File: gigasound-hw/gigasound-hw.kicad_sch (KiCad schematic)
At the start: 14 parts, among them J1 Conn_01x04_Socket, J2 Conn_01x05_Socket, SW1 PLAY, SW2 STOP, SW3 MODE, U1 STM32F401RETx, Y1 8MHz

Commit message: progress hw schematic
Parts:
- removed SW3: MODE, symbol Switch:SW_Push
- added C10: C, symbol Device:C
- added C11, C3, C4, C5, C6, C7, C8, C9: 100nF, symbol Device:C
- added C12: 4.7uF, symbol Device:C
- added J3: Conn_01x05_Socket, symbol Connector:Conn_01x05_Socket
- added L1: 600R, symbol Device:L
- added R3, R4, R5, R6: 10K, symbol Device:R
- added SW4: STOP, symbol Switch:SW_Push
- added SW5: MODE, symbol Switch:SW_Push
- added TPA8, TPB1, TPB10, TPB12, TPB2, TPB3, TPB4, TPB5, TPB8, TPB9, TPC0, TPC1, TPC10, TPC11, TPC12, TPC13, TPC14, TPC15, TPC2, TPC3, TPC6, TPC7, TPC8, TPC9, TPD2: ~, TestPoint:TestPoint_Pad_D1.0mm, symbol Connector:TestPoint
- SW2: value STOP -> 100nF
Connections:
- net GND: now also D1.3 (VSS), SW1.1, SW2.1, U1.12 (VSSA), U1.18 (VSS), U1.31 (VSS), U1.47 (VSS), U1.63 (VSS), C10.1, C11.1, C12.1, C3.2, C4.2, C5.2, J3.GND, R6.1, SW4.1, SW5.1
- net 5V: now reaches D1.1 (VDD)
- net LED: now reaches D1.4 (DIN)
- net LED: now also U1.50 (PA15)
- net PLAY: now reaches SW1.2
- net PLAY: now also U1.34 (PB13), C3.1
- net at SW2.2: now also U1.7 (NRST), C10.2
- net at R1.1: now also R3.2
- net at U1.1 (VBAT): now also U1.19 (VDD), U1.32 (VDD), U1.48 (VDD), U1.64 (VDD), C6.2, C7.2, C8.2, C9.2
- net at U1.10 (PC2): now also TPC2.1
- net at U1.11 (PC3): now also TPC3.1
- net VDDA: now reaches U1.13 (VREF+)
- net VDDA: now also C11.2, L1.1
- net ADC_CH0: now reaches U1.14 (PA0)
- net ADC_CH1: now reaches U1.15 (PA1)
- net ADC_CH2: now reaches U1.16 (PA2)
- net ADC_CH3: now reaches U1.17 (PA3)
- net at U1.2 (PC13): now also TPC13.1
- net ADC_CH4: now reaches U1.20 (PA4)
- net ADC_CH5: now reaches U1.21 (PA5)
- net ADC_CH6: now reaches U1.22 (PA6)
- net ADC_CH7: now reaches U1.23 (PA7)
- net ADC_CH14: now reaches U1.24 (PC4)
- net ADC_CH15: now reaches U1.25 (PC5)
- net ADC_CH8: now reaches U1.26 (PB0)
- net at U1.27 (PB1): now also TPB1.1
- net at U1.28 (PB2): now also TPB2.1
- net at U1.29 (PB10): now also TPB10.1
- net at U1.3 (PC14): now also TPC14.1
- net at U1.30 (VCAP1): now also C12.2
- net at U1.33 (PB12): now also TPB12.1
- net STOP: now reaches U1.35 (PB14)
- net STOP: now also C4.1, SW4.2
- net MODE: now reaches U1.36 (PB15)
- net MODE: now also C5.1, SW5.2
- net at U1.37 (PC6): now also TPC6.1
- net at U1.38 (PC7): now also TPC7.1
- net at U1.39 (PC8): now also TPC8.1
- net at U1.4 (PC15): now also TPC15.1
- net at U1.40 (PC9): now also TPC9.1
- net at U1.41 (PA8): now also TPA8.1
- net TX: now reaches U1.42 (PA9)
- net TX: now also J3.TX
- net RX: now reaches U1.43 (PA10)
- net RX: now also J3.RX
- net USB_DM: now reaches U1.44 (PA11)
- net USB_DP: now reaches U1.45 (PA12)
- net SWDIO: now reaches U1.46 (PA13)
- net SWDIO: now also J3.SWDIO
- net SWCLK: now reaches U1.49 (PA14)
- net SWCLK: now also J3.SWCLK
- net at U1.51 (PC10): now also TPC10.1
- net at U1.52 (PC11): now also TPC11.1
- net at U1.53 (PC12): now also TPC12.1
- net at U1.54 (PD2): now also TPD2.1
- net at U1.55 (PB3): now also TPB3.1
- net at U1.56 (PB4): now also TPB4.1
- net at U1.57 (PB5): now also TPB5.1
- net SCL: now reaches U1.58 (PB6)
- net SCL: now also R5.2
- net SDA: now reaches U1.59 (PB7)
- net SDA: now also R4.2
- net at U1.60 (BOOT0): now also R6.2
- net at U1.61 (PB8): now also TPB8.1
- net at U1.62 (PB9): now also TPB9.1
- net at U1.8 (PC0): now also TPC0.1
- net at U1.9 (PC1): now also TPC1.1
- new net 3.3V: C6.1, C7.1, C8.1, C9.1, L1.2, R3.1, R4.1, R5.1
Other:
- note added: "UART DEBUG PORT PROGRAMMING PORT"
- company: (none) -> Poliba
- title: (none) -> GigaSound-MIDI
- moved on the sheet: C1, C2, D1, J2, R1, R2, SW1, Y1

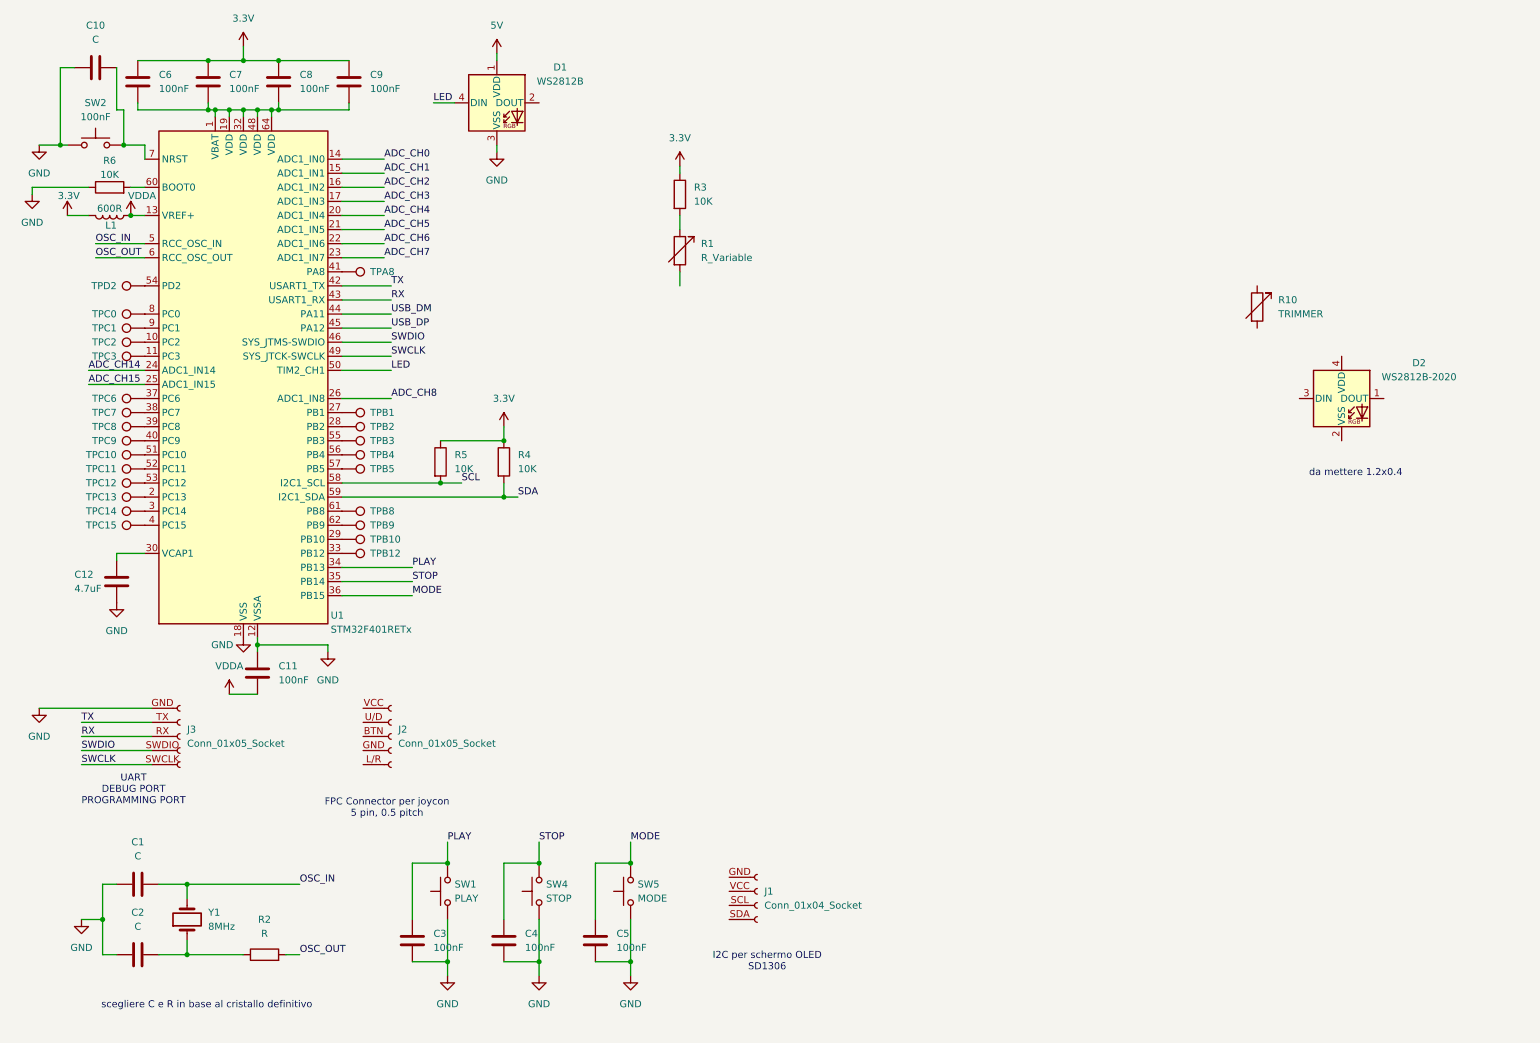
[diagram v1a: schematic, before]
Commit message: hw: added usb, 3.3v, cleaned up
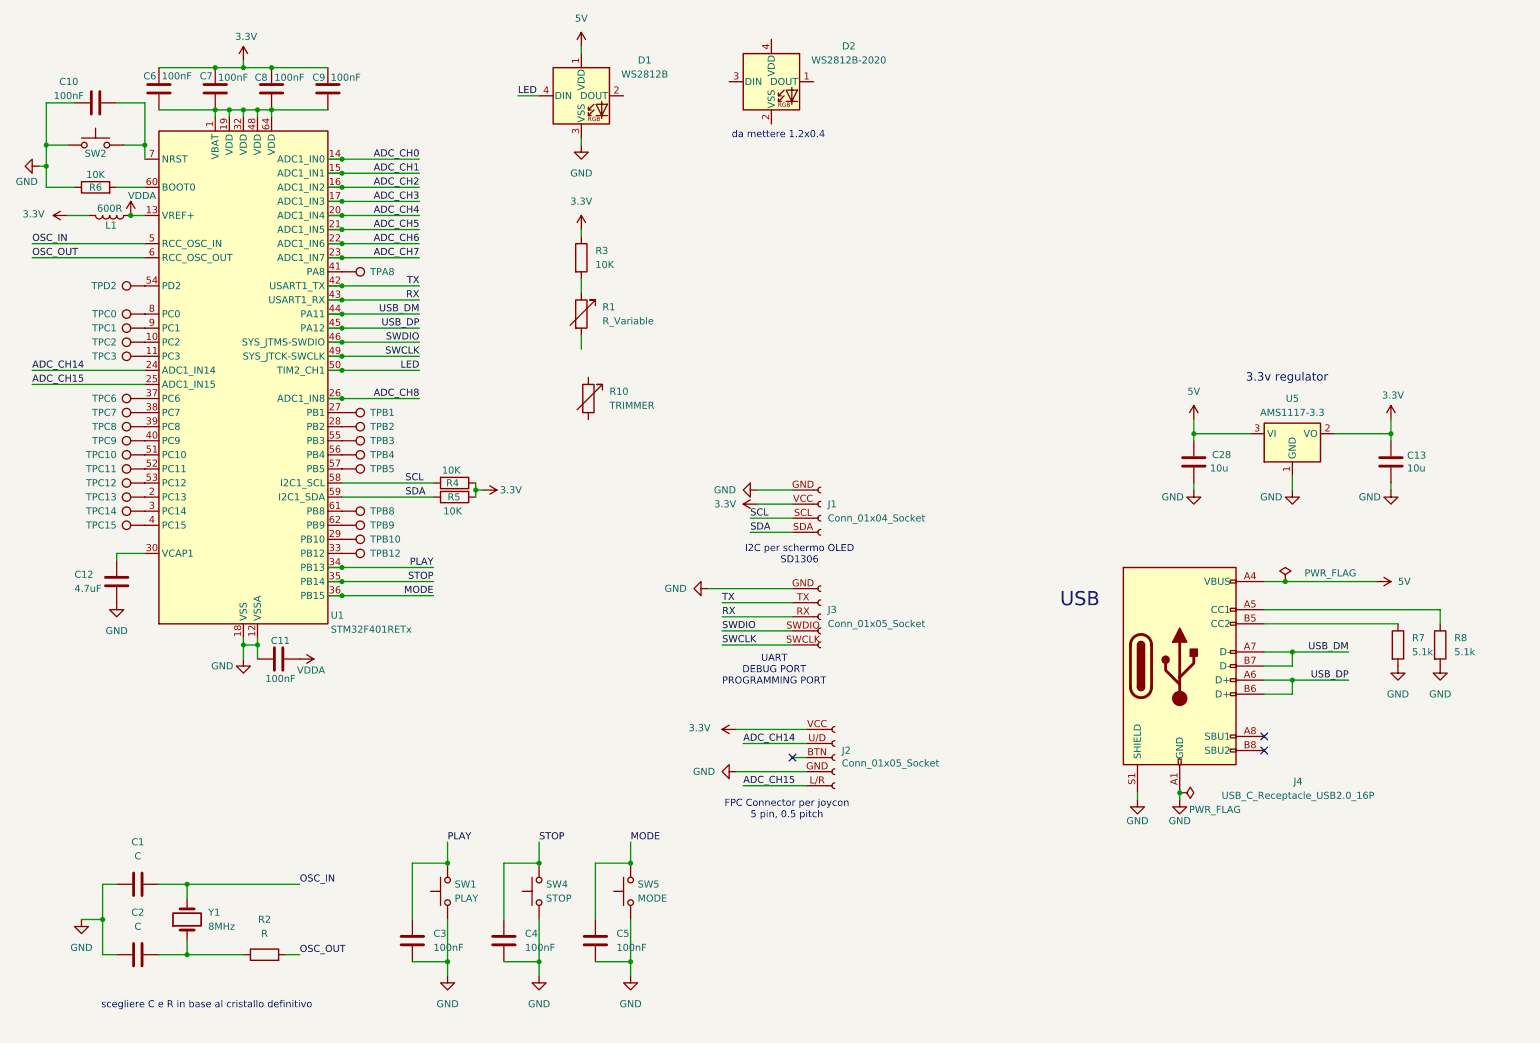
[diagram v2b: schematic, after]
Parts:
- added C13, C28: 10u, Capacitor_SMD:C_0402_1005Metric_Pad0.74x0.62mm_HandSolder, symbol Device:C
- added J4: USB_C_Receptacle_USB2.0_16P, Connector_USB:USB_C_Receptacle_G-Switch_GT-USB-7010ASV, symbol Connector:USB_C_Receptacle_USB2.0_16P
- added R7, R8: 5.1k, Resistor_SMD:R_0402_1005Metric_Pad0.72x0.64mm_HandSolder, symbol Device:R
- added U5: AMS1117-3.3, Package_TO_SOT_SMD:SOT-223-3_TabPin2, symbol Regulator_Linear:AMS1117-3.3
- C10: value C -> 100nF
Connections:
- net 3.3V: now also J1.VCC, J2.VCC, C13.1, U5.2 (VO)
- net 5V: now also C28.1, J4.A4 (VBUS), J4.A9 (VBUS), J4.B4 (VBUS), J4.B9 (VBUS), U5.3 (VI)
- net ADC_CH14: now also J2.U/D (UP/DOWN)
- net ADC_CH15: now also J2.L/R (LEFT/RIGHT)
- net GND: now also J1.GND, J2.GND, C13.2, C28.2, J4.A1 (GND), J4.A12 (GND), J4.B1 (GND), J4.B12 (GND), J4.S1 (SHIELD), R7.2, R8.2, U5.1 (GND)
- net SCL: now also J1.SCL
- net SDA: now also J1.SDA
- net USB_DM: now also J4.A7 (D-), J4.B7 (D-)
- net USB_DP: now also J4.A6 (D+), J4.B6 (D+)
- new net: J4.B5 (CC2), R7.1
- new net: J4.A5 (CC1), R8.1
- no-connect marks 0 -> 3
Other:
- note added: "3.3v regulator"
- note added: "USB"
- moved on the sheet: C10, C11, C6, C7, C8, C9, D1, D2, J1, J2, J3, R1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

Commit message: working ws2812
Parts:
- removed TPC12: ~, TestPoint:TestPoint_Pad_D1.0mm, symbol Connector:TestPoint
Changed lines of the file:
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@@
-	)
-	(symbol
-		(lib_id "Connector:TestPoint")
-		(at 36.83 97.79 90)
-		(unit 1)
-		(exclude_from_sim no)
-		(in_bom yes)
-		(on_board yes)
-		(dnp no)
-		(property "Reference" "TPC12"
-			(at 31.75 97.79 90)
-			(effects
-				(font
-					(size 1.27 1.27)
-				)
-				(justify left)
-			)
-		)
-		(property "Value" "~"
-			(at 31.75 96.52 90)
-			(effects
-				(font
-					(size 1.27 1.27)
-				)
-				(justify left)
-			)
-		)
-		(property "Footprint" "TestPoint:TestPoint_Pad_D1.0mm"
-			(at 36.83 92.71 0)
-			(effects
-				(font
-					(size 1.27 1.27)
-				)
-				(hide yes)
-			)
-		)
-		(property "Datasheet" "~"
-			(at 36.83 92.71 0)
-			(effects
-				(font
-					(size 1.27 1.27)
-				)
-				(hide yes)
-			)
-		)
-		(property "Description" "test point"
-			(at 36.83 97.79 0)
-			(effects
-				(font
-					(size 1.27 1.27)
-				)
-				(hide yes)
-			)
-		)
-		(pin "1"
-		)
-		(instances
-			(project "gigasound-hw"
-				(path "/8926df81-91df-4835-b346-b30b02cc5690"
-					(reference "TPC12")
-					(unit 1)
-				)
-			)
-		)
 	)
 	(symbol
@@
 		)
 		(pin "53"
+			(alternate "SPI3_MOSI")
 		)
 		(pin "25"

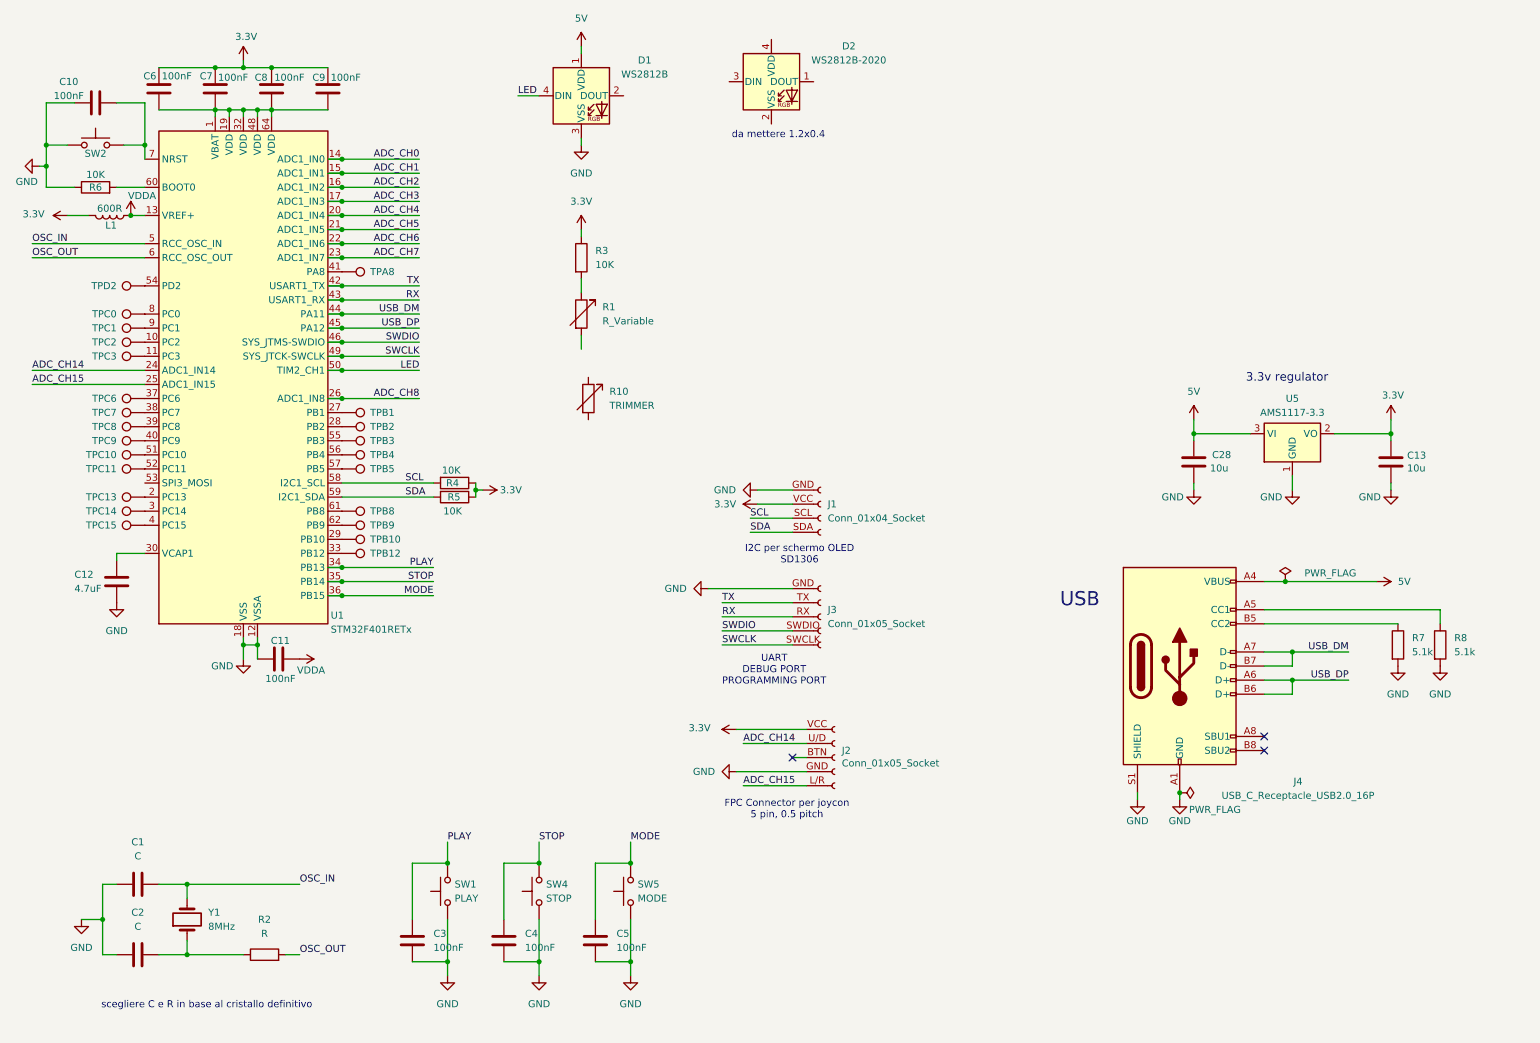
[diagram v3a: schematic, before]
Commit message: add led to sch
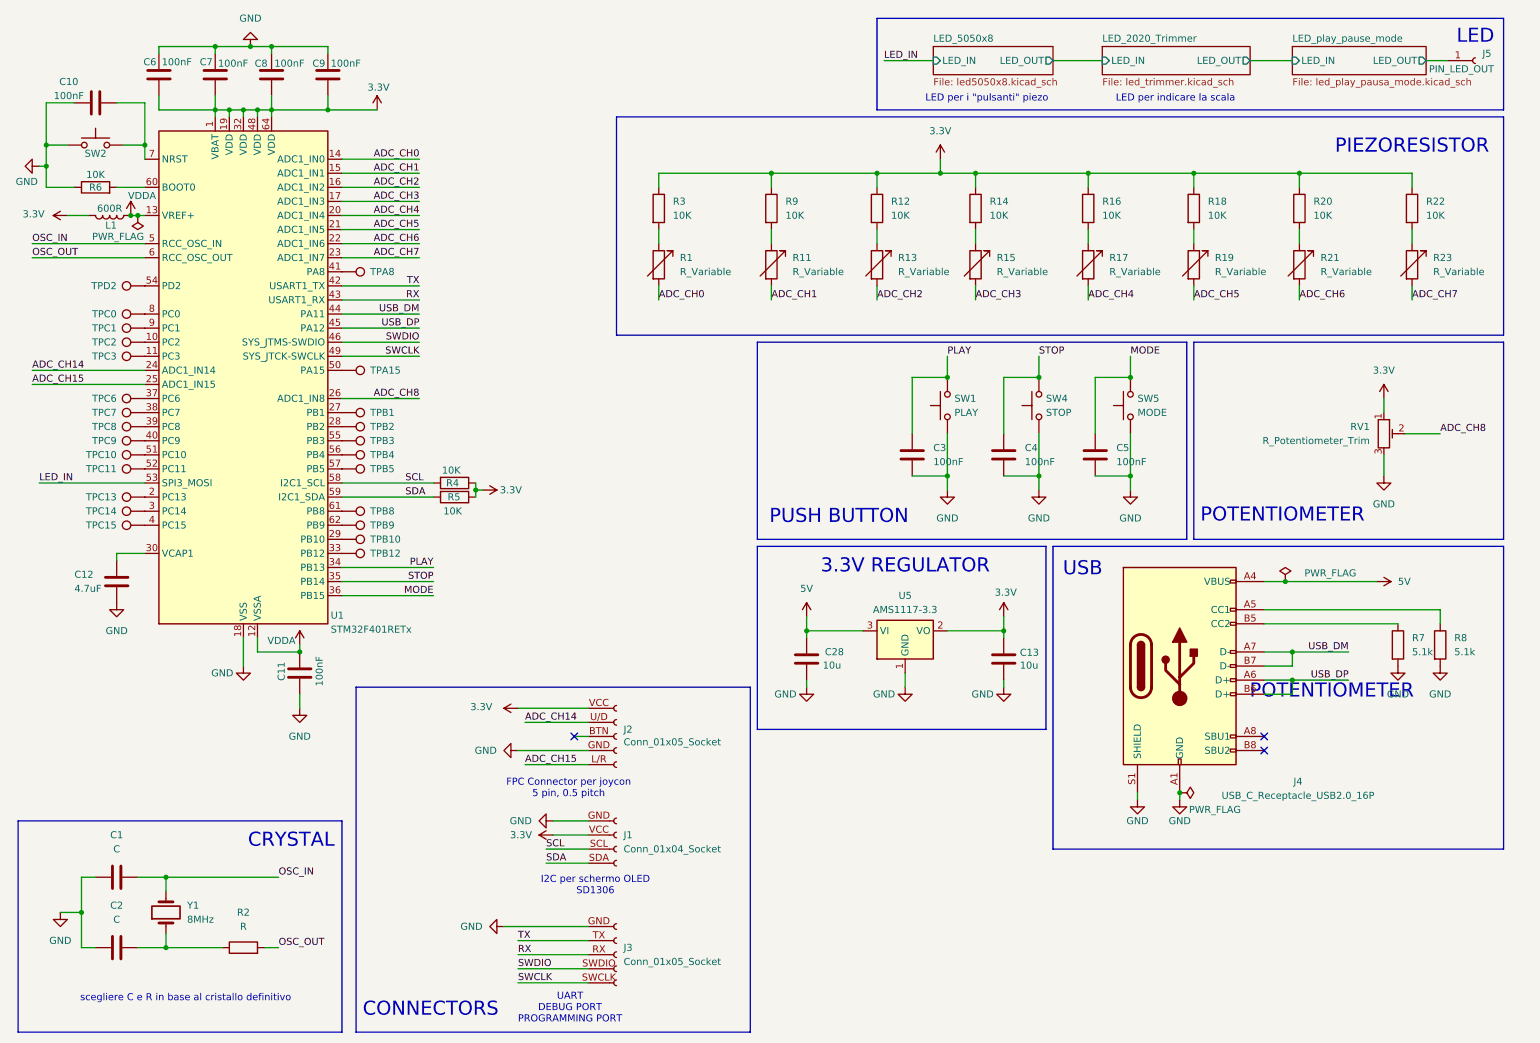
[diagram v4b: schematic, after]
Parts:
- removed D1: WS2812B, LED_SMD:LED_WS2812B_PLCC4_5.0x5.0mm_P3.2mm, symbol LED:WS2812B
- removed D2: WS2812B-2020, LED_SMD:LED_WS2812B-2020_PLCC4_2.0x2.0mm, symbol LED:WS2812B-2020
- removed R10: TRIMMER, symbol Device:R_Variable
- added J5: PIN_LED_OUT, Connector_PinHeader_1.00mm:PinHeader_1x01_P1.00mm_Vertical, symbol Connector:Conn_01x01_Socket
- added R11, R13, R15, R17, R19, R21, R23: R_Variable, symbol Device:R_Variable
- added R12, R14, R16, R18, R20, R22, R9: 10K, symbol Device:R
- added RV1: R_Potentiometer_Trim, Potentiometer_THT:Potentiometer_Piher_PT-10-V10_Vertical, symbol Device:R_Potentiometer_Trim
- added TPA15: ~, TestPoint:TestPoint_Pad_D1.0mm, symbol Connector:TestPoint
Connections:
- net 3.3V: now also C6.2, C7.2, C8.2, C9.2, U1.1 (VBAT), U1.19 (VDD), U1.32 (VDD), U1.48 (VDD), U1.64 (VDD), R12.1, R14.1, R16.1, R18.1, R20.1, R22.1, R9.1, RV1.1; no longer C6.1, C7.1, C8.1, C9.1
- net ADC_CH0: now also R1.2
- net ADC_CH1: now also R11.2
- net ADC_CH2: now also R13.2
- net ADC_CH3: now also R15.2
- net ADC_CH4: now also R17.2
- net ADC_CH5: now also R19.2
- net ADC_CH6: now also R21.2
- net ADC_CH7: now also R23.2
- net ADC_CH8: now also RV1.2
- net GND: now also C6.1, C7.1, C8.1, C9.1, RV1.3; no longer U1.12 (VSSA)
- net VDDA: now also U1.12 (VSSA)
- net LED_IN: now reaches U1.53 (PC12)
- net LED: no longer names the net of U1.50 (PA15)
- net LED: now also TPA15.1
- new net: R20.2, R21.1
- new net: R16.2, R17.1
- new net: R22.2, R23.1
- new net: R18.2, R19.1
- new net: R12.2, R13.1
- new net: R11.1, R9.2
- new net: R14.2, R15.1
- new net LED_play_pause_mode/LED_OUT: J5.1 (Pin_1)
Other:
- added sheet LED_2020_Trimmer (led_trimmer.kicad_sch)
- added sheet LED_5050x8 (led5050x8.kicad_sch)
- added sheet LED_play_pause_mode (led_play_pausa_mode.kicad_sch)
- note added: "3.3V REGULATOR"
- note added: "CONNECTORS"
- note added: "CRYSTAL"
- note added: "LED"
- note added: "LED per i "pulsanti" piezo"
- note added: "LED per indicare la scala"
- note added: "PIEZORESISTOR"
- note added: "POTENTIOMETER"
- note added: "PUSH BUTTON"
- note removed: "3.3v regulator"
- note removed: "da mettere 1.2x0.4"
- moved on the sheet: C1, C11, C13, C2, C28, C3, C4, C5, C6, C7, C8, C9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
